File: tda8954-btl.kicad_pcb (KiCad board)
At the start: 2 copper layers, 100 x 48 mm, 89 parts, among them J1 Screw_Terminal_01x02, J10 Conn_01x01_Male, J2 Conn_01x01_Male, J3 Screw_Terminal_01x02, J4 Conn_01x01_Male, J5 Conn_01x01_Male, J6 Screw_Terminal_01x02, J7 Screw_Terminal_01x03, J8 Conn_01x01_Male, J9 Conn_01x01_Male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

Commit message: polishing; completed first pass layout
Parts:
- removed J3: Screw_Terminal_01x02, Terminals_Phoenix:TerminalBlock_Phoenix_MKDS1.5-2pol
- J10: footprint power:FASTON250P_5.08mm_male_vertical -> Mounting_Holes:MountingHole_3.2mm_M3_DIN965_Pad
- moved J10 48.1 mm to (29.0, 29.0)
- moved C36 48.0 mm to (33.6, 26.2), turned to 0 degrees
- moved C12 4.11 mm to (94.8, 50.1), turned to 180 degrees
- moved R21 3.56 mm to (91.0, 50.1)
- moved R5 2.54 mm to (94.0, 55.2)
- moved R16 1.78 mm to (68.1, 64.1)
- moved D2 1.50 mm to (68.0, 59.8)
- moved R9 1.02 mm to (88.5, 53.4)
- moved Q1 0.76 mm to (87.2, 49.8)
- moved R10 0.51 mm to (83.9, 53.4)
- moved R13 0.51 mm to (85.9, 53.4)
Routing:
- net /GND: track 243.5 -> 273.7 mm
- net /HTSNK: track 10.2 -> 5.41 mm
- net Net-(D1-Pad1): track 33.3 -> 31.5 mm, vias 3 -> 1
- net Net-(C12-Pad2): track 3.81 -> 5.53 mm
- net /OUT2: track 67.3 -> 65.8 mm
- net /INM: track 58.5 -> 57.1 mm
- net Net-(Q1-Pad3): track 12.3 -> 13.8 mm
- net /INP: track 69.4 -> 70.5 mm
- net Net-(Q2-Pad3): track 12.0 -> 13.0 mm
- net /DIAG2: track 60.9 -> 61.8 mm
- net /TFB: track 60.9 -> 61.7 mm
- net /VDD: track 219.9 -> 219.1 mm
- net Net-(J6-Pad1): track 3.37 -> 4.11 mm
- net Net-(D2-Pad1): track 3.75 -> 3.12 mm
- net Net-(C7-Pad2): track 16.4 -> 15.8 mm
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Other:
- board text added: "HEAT SINK"
- board text added: "INPUT"
- board text added: "OUT+"
- board text added: "OUT-"
- board text added: "POWER"
- board text removed: "Input"
- board text removed: "Unmute"

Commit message: polishing, plotted gerbers
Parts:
- added R23: 20, Resistors_SMD:R_0805, F.Cu at (95.5, 31.8)
- added R24: 20, Resistors_SMD:R_0805, F.Cu at (94.2, 28.2)
- added REF**: Tyrrell Zaibatsu, tz:Tyrrell-Zaibatsu-20-Back, F.Cu at (81.0, 45.0)
- added REF**: Tyrrell Zaibatsu, tz:Tyrrell-Zaibatsu-10, F.Cu at (45.3, 39.7)
- added REF***: OSHW-Logo2_7.3x6mm_SilkScreen, Symbols:OSHW-Logo2_7.3x6mm_SilkScreen, F.Cu at (119.5, 62.7)
- added REF***: OSHW-Symbol_6.7x6mm_SilkScreen, pcb:OSHW-Symbol_6.7x6mm_BackSilkScreen, F.Cu at (42.0, 41.0)
- J10: footprint Mounting_Holes:MountingHole_3.2mm_M3_DIN965_Pad -> power:FASTON250P_5.08mm_male_vertical
- R1, R6: value 10 -> 20
- R12, R18, R19: value 1k -> 3k9
- moved FID2 17.7 mm to (46.0, 69.0)
- moved FID1 8.54 mm to (113.0, 61.0)
- moved J5 5.12 mm to (29.8, 42.0)
- moved J8 5.12 mm to (29.8, 50.8)
- moved J9 5.12 mm to (29.8, 59.7)
- moved J7 5.08 mm to (29.8, 45.8)
- moved FID4 5.00 mm to (59.0, 27.0)
- moved C36 1.96 mm to (35.6, 26.2)
- moved C4 1.84 mm to (92.2, 33.8)
- moved C27 1.52 mm to (53.2, 29.0)
- moved C26 1.52 mm to (42.0, 29.0)
- moved R1 1.30 mm to (95.5, 33.8), turned to 180 degrees
- moved C12 1.27 mm to (94.8, 51.4)
- moved J10 1.24 mm to (29.2, 30.2), turned to 180 degrees
- moved L3 1.14 mm to (116.9, 34.1)
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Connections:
- net /TFB renamed /DIAG1
- U1 pad 17: (no net) -> /GND
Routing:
- net /VDD: track 219.1 -> 207.0 mm
- net /VSS: track 201.8 -> 208.7 mm
- net Net-(C13-Pad1): track 9.79 -> 15.5 mm
- net /HTSNK: track 5.41 -> 11.0 mm
- net /GND: track 273.7 -> 279.0 mm
- net /OP1: track 65.8 -> 69.2 mm
- net Net-(D1-Pad1): track 31.5 -> 29.2 mm, vias 1 -> 2
- net Net-(C3-Pad1): track 4.46 -> 6.17 mm
- net Net-(C12-Pad2): track 5.53 -> 3.92 mm
- net Net-(J6-Pad1): track 4.11 -> 5.61 mm
- net Net-(J6-Pad2): track 7.75 -> 8.77 mm
- net /OP2: track 46.3 -> 47.3 mm
- net /INP: track 70.5 -> 69.5 mm
- net Net-(C6-Pad1): track 3.31 -> 2.42 mm
- net /MODE: track 7.83 -> 7.07 mm
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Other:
- board text added: "TDA8954 BTL 400W/8R"
- board text added: "TDA8954 BTL 400W/8R Rev.A 202111 william@brodie-tyrrell.org github.com/phenidone"
- board text added: "VDD +41V"
- board text added: "VSS -41V"
- board text removed: "POWER"
- board text removed: "VDD"
- board text removed: "VSS"

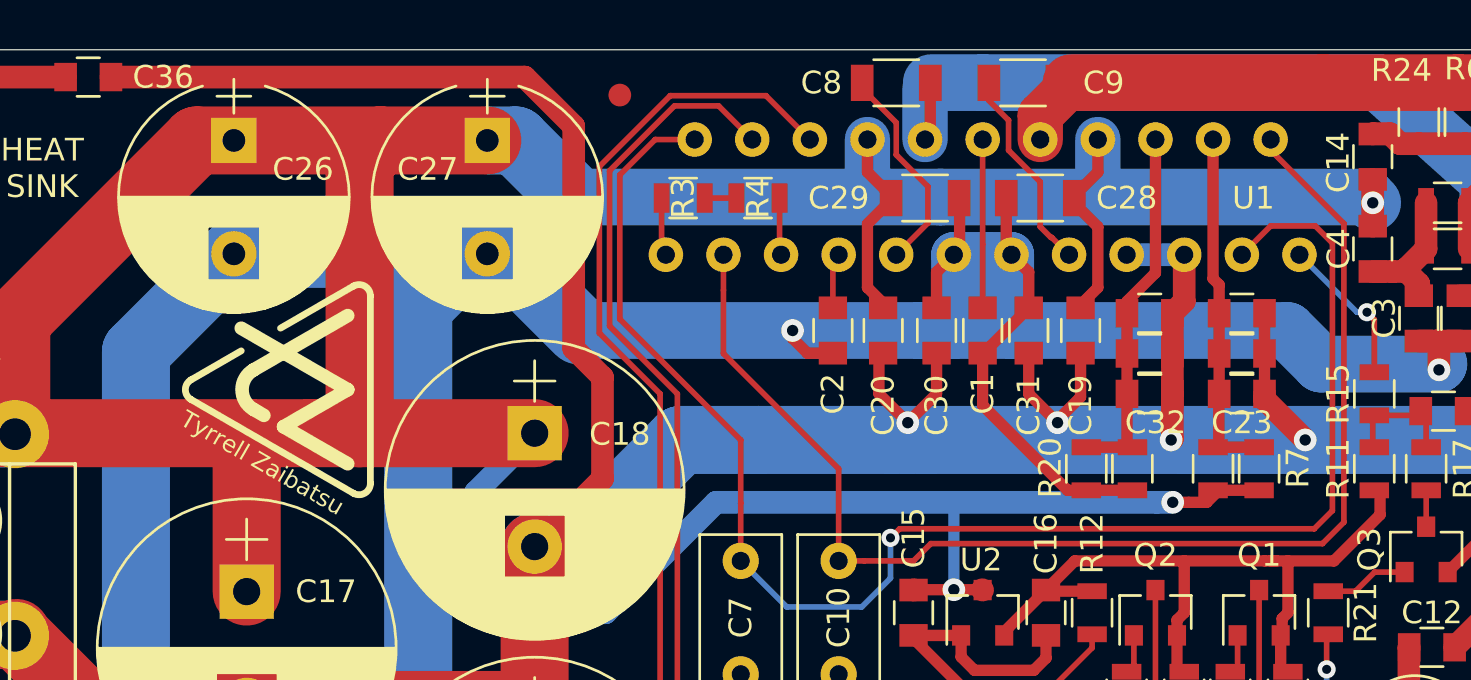
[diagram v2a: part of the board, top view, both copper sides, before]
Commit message: fixed footprints, re-plotted
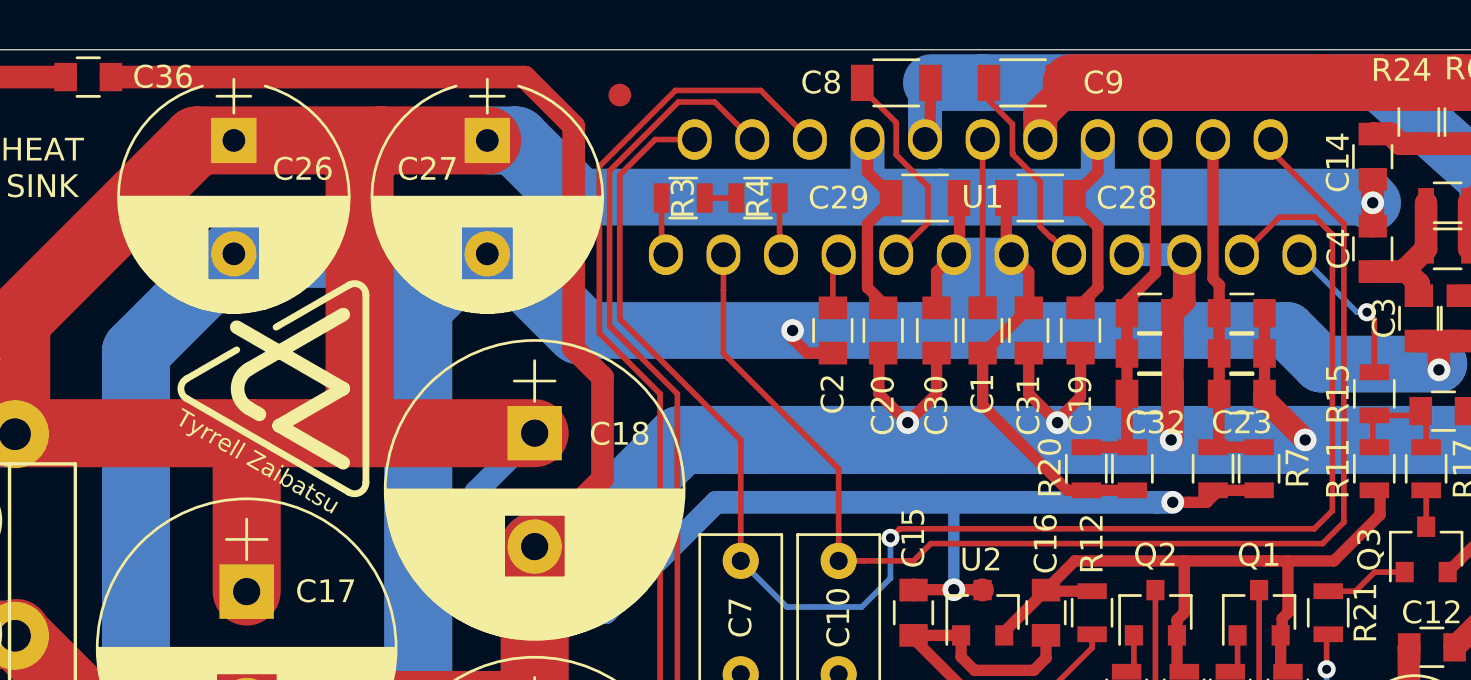
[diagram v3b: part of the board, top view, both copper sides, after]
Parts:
- moved REF** 0.20 mm to (45.1, 39.6)
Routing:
- net /INP: track 69.5 -> 70.1 mm
- net /OSC: track 2.84 -> 2.31 mm
